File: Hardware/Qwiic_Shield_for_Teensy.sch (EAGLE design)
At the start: 21 parts, among them J1 QWIIC_RA, J2 QWIIC_RA, J3 QWIIC_Vertical, J4 QWIIC_Vertical, J5 ALT PWR

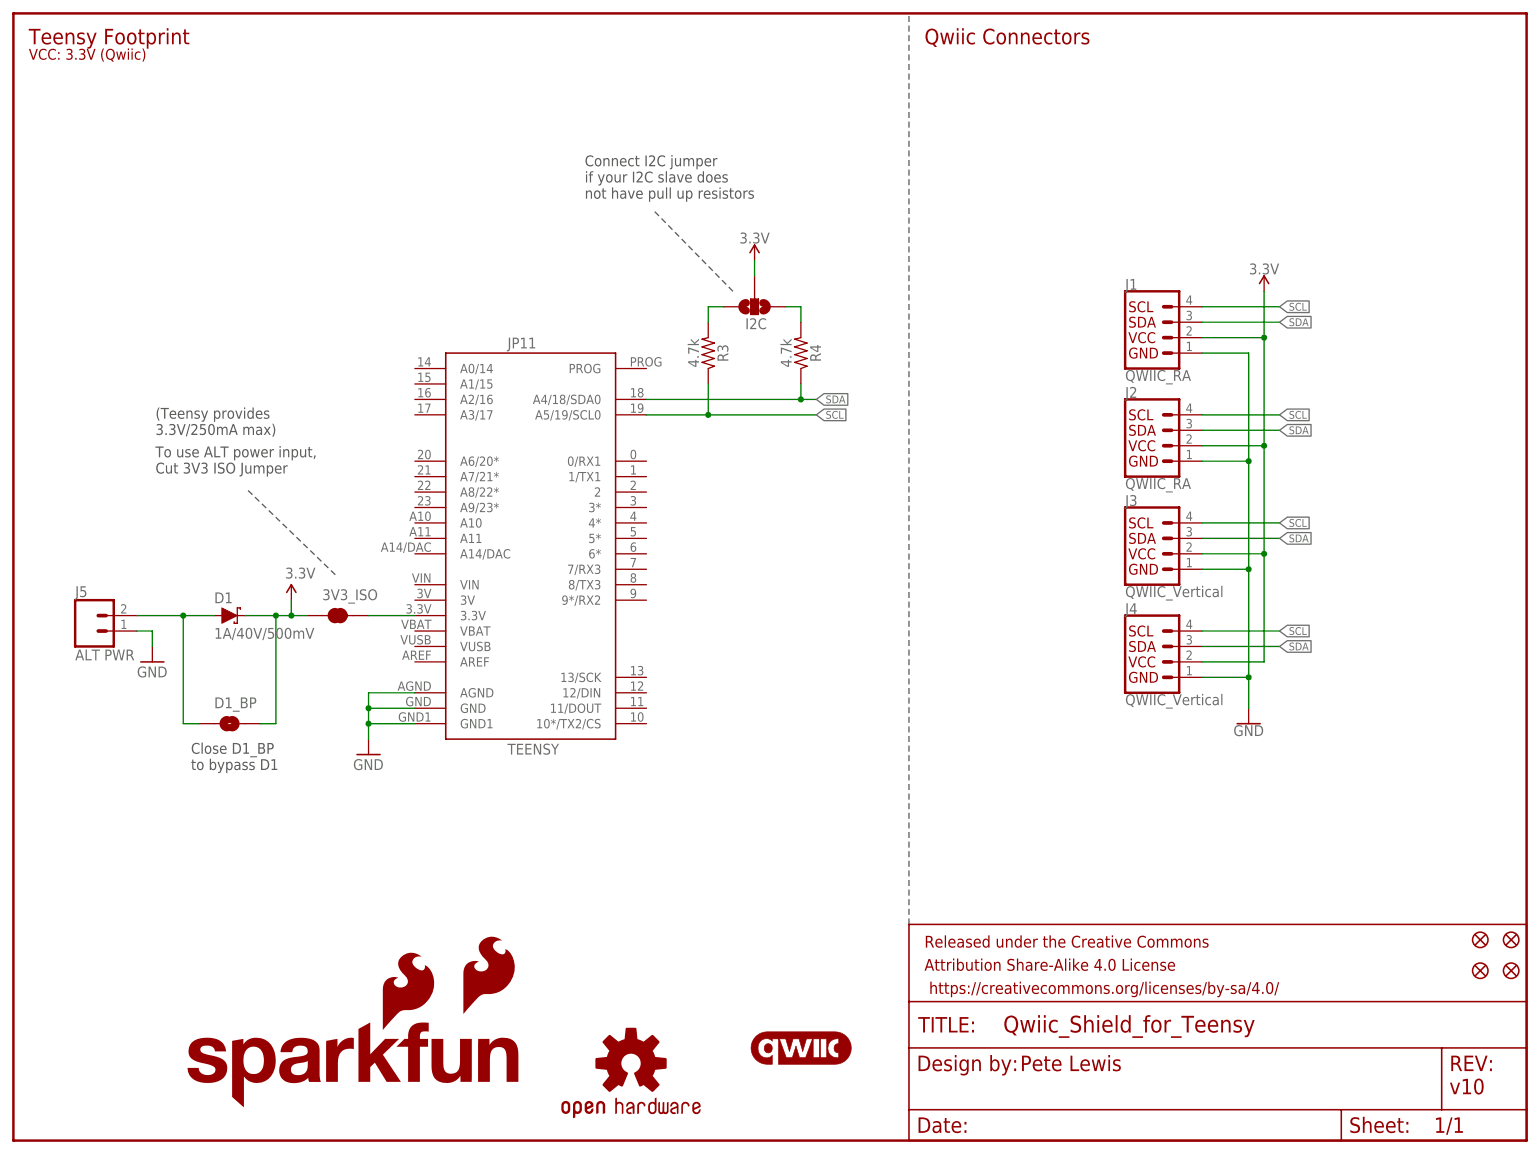
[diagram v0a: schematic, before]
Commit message: Routing done
-added diode on ALT 3V3 input
-added PRG button for easier access to programming button
-added prototyping area (with vscore) to extend this to also fit longer teensy board form factors
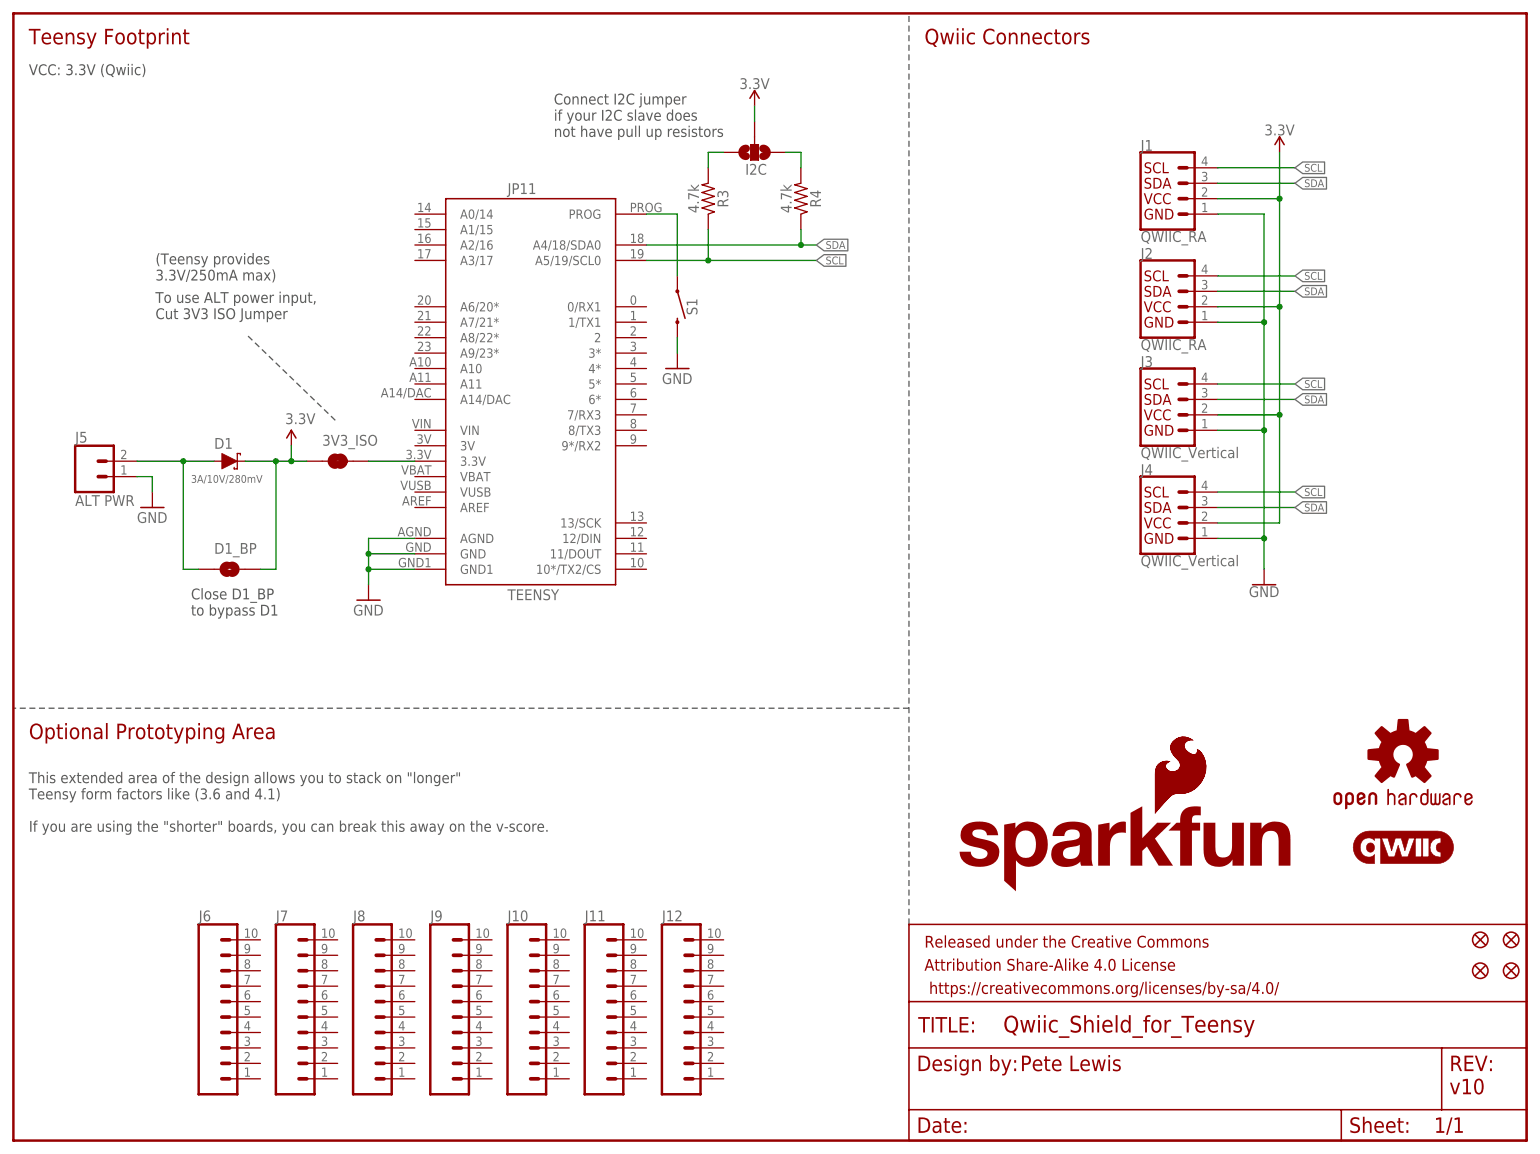
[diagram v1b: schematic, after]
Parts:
- added J10, J11, J12, J6, J7, J8, J9: (no value), SparkFun-Connectors:CONN_10NO_SILK_PTH_FEMALE
- added S1: MOMENTARY-SWITCH-SPST-SMD-5.2MM-TALL, SparkFun-Switches:MOMENTARY-SWITCH-SPST-SMD-5.2MM-TALL
- D1: value 1A/40V/500mV -> 3A/10V/280mV; device SparkFun-DiscreteSemi:DIODE-SCHOTTKY-SS14 -> SparkFun-DiscreteSemi:DIODE-SCHOTTKY-BAT60A
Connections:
- new net N$5: JP11.PROG, S1.1
- net GND: now also S1.2
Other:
- note added: "Optional Prototyping Area"
- note added: "This extended area of the design allows you to stack on "longer" Teensy form factors like (3.6 and 4.1) If you are using the "shorter" boards, you can break this away on the v-score."
- moved on the sheet: 3V3_ISO, D1, D1_BP, I2C, J1, J2, J3, J4, J5, JP11, R3, R4

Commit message: Teensy FP library update
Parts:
- JP11: device Testing:TEENSY-3.1NOSILK -> SparkFun-Boards:TEENSY-3.1NOSILK
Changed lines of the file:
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@@
 <part name="FD3" library="SparkFun-Aesthetics" deviceset="FIDUCIAL" device="1X2"/>
 <part name="FD4" library="SparkFun-Aesthetics" deviceset="FIDUCIAL" device="1X2"/>
-<part name="JP11" library="Testing" deviceset="TEENSY-3.1" device="NOSILK" value="TEENSY"/>
+<part name="JP11" library="SparkFun-Boards" deviceset="TEENSY-3.1" device="NOSILK" value="TEENSY"/>
 <part name="GND3" library="SparkFun-Aesthetics" deviceset="GND" device=""/>
 <part name="SUPPLY7" library="SparkFun-Aesthetics" deviceset="3.3V" device=""/>
@@
 <segment>
 <pinref part="JP11" gate="G$1" pin="GND"/>
-<wire x1="66.04" y1="96.52" x2="58.42" y2="96.52" width="0.1524" layer="91"/>
+<wire x1="68.58" y1="96.52" x2="58.42" y2="96.52" width="0.1524" layer="91"/>
 <wire x1="58.42" y1="96.52" x2="58.42" y2="93.98" width="0.1524" layer="91"/>
 <pinref part="JP11" gate="G$1" pin="GND1"/>
 <wire x1="58.42" y1="93.98" x2="58.42" y2="91.44" width="0.1524" layer="91"/>
-<wire x1="66.04" y1="93.98" x2="58.42" y2="93.98" width="0.1524" layer="91"/>
+<wire x1="68.58" y1="93.98" x2="58.42" y2="93.98" width="0.1524" layer="91"/>
 <junction x="58.42" y="93.98"/>
 <pinref part="GND3" gate="1" pin="GND"/>
 <pinref part="JP11" gate="G$1" pin="AGND"/>
-<wire x1="66.04" y1="99.06" x2="58.42" y2="99.06" width="0.1524" layer="91"/>
+<wire x1="68.58" y1="99.06" x2="58.42" y2="99.06" width="0.1524" layer="91"/>
 <wire x1="58.42" y1="99.06" x2="58.42" y2="96.52" width="0.1524" layer="91"/>
 <junction x="58.42" y="96.52"/>
@@
 </segment>
 <segment>
-<wire x1="104.14" y1="147.32" x2="129.54" y2="147.32" width="0.1524" layer="91"/>
+<wire x1="101.6" y1="147.32" x2="129.54" y2="147.32" width="0.1524" layer="91"/>
 <pinref part="R4" gate="G$1" pin="1"/>
 <wire x1="129.54" y1="147.32" x2="132.08" y2="147.32" width="0.1524" layer="91"/>
@@
 </segment>
 <segment>
-<wire x1="104.14" y1="144.78" x2="114.3" y2="144.78" width="0.1524" layer="91"/>
+<wire x1="101.6" y1="144.78" x2="114.3" y2="144.78" width="0.1524" layer="91"/>
 <pinref part="R3" gate="G$1" pin="1"/>
 <wire x1="114.3" y1="144.78" x2="132.08" y2="144.78" width="0.1524" layer="91"/>
@@
 <pinref part="JP11" gate="G$1" pin="3.3V"/>
 <pinref part="3V3_ISO" gate="G$1" pin="2"/>
-<wire x1="58.42" y1="111.76" x2="66.04" y2="111.76" width="0.1524" layer="91"/>
+<wire x1="58.42" y1="111.76" x2="68.58" y2="111.76" width="0.1524" layer="91"/>
 </segment>
 </net>
@@
 <segment>
 <pinref part="JP11" gate="G$1" pin="PROG"/>
-<wire x1="104.14" y1="152.4" x2="109.22" y2="152.4" width="0.1524" layer="91"/>
+<wire x1="101.6" y1="152.4" x2="109.22" y2="152.4" width="0.1524" layer="91"/>
 <pinref part="S1" gate="G$1" pin="1"/>
 <wire x1="109.22" y1="152.4" x2="109.22" y2="142.24" width="0.1524" layer="91"/>
